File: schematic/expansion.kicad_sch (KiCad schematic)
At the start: 21 parts, among them J8 EXPANSION, U10 TPD4E05U06DQA, U11 TPD4E05U06DQA, U12 TPD4E05U06DQA, U13 TPD4E05U06DQA, U6 TPD4E05U06DQA, U7 TPD4E05U06DQA, U8 TPD4E05U06DQA, U9 TPD4E05U06DQA

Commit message: Rework for 8 nodes with MCP23017 relay drive
Target is now 8 motherboards per frame (was 14 in the schematic).

- relays_a/relays_b (14 channels, 28 photoMOS) replaced by one
  'Relay channels' sheet: 8 channels, 16 TLP176AM, J11-J18, same
  per-channel circuit and parts.
- U14 MCP23017 @0x20 drives the LEDs: GPA0-7 = PWR_DRV1-8,
  GPB0-7 = RST_DRV1-8. R32 pulls EXP_nRESET low so U14 stays in
  reset (all buttons released) unless the MCU drives it; R33 pulls
  up the shared open-drain EXP_INT.
- MCU: the two 14-bit drive buses are gone; PE2 = EXP_nRESET,
  PE3 = EXP_INT, the other 26 freed pins are no-connect.
- Expansion header J8 grows to 2x20 and carries I2C1, EXP_nRESET
  and EXP_INT (pins 5-8) for extra expander modules or a later
  power board, plus 3V3/5V on both ends.
- Net classes for the second relay bank removed; drive patterns
  point at the new sheet. Board regenerated (nothing placed).
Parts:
- removed J8: EXPANSION, Connector_PinHeader_2.54mm:PinHeader_2x18_P2.54mm_Vertical, symbol Connector_Generic:Conn_02x18_Odd_Even
- added J8: EXPANSION, Connector_PinHeader_2.54mm:PinHeader_2x20_P2.54mm_Vertical, symbol Connector_Generic:Conn_02x20_Odd_Even
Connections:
- net GND: now also J8.3 (Pin_3), J8.37 (Pin_37), J8.38 (Pin_38), J8.4 (Pin_4)
- net GPIO_PA0: now also RN2.8 (R1.2); no longer RN1.8 (R1.2)
- net GPIO_PA10: now also RN6.5 (R4.2); no longer RN6.7 (R2.2)
- net GPIO_PA15: now also RN5.5 (R4.2); no longer RN4.5 (R4.2)
- net GPIO_PA3: now also RN2.7 (R2.2); no longer RN1.7 (R2.2)
- net GPIO_PA4: now also RN2.6 (R3.2); no longer RN1.6 (R3.2)
- net GPIO_PA6: now also RN2.5 (R4.2); no longer RN1.5 (R4.2)
- net GPIO_PA8: now also RN6.6 (R3.2); no longer RN6.8 (R1.2)
- net GPIO_PB1: now also RN3.8 (R1.2); no longer RN2.8 (R1.2)
- net GPIO_PB10: now also RN7.6 (R3.2); no longer RN7.8 (R1.2)
- net GPIO_PB13: now also RN7.5 (R4.2); no longer RN7.7 (R2.2)
- net GPIO_PB14: now also RN8.8 (R1.2); no longer RN7.6 (R3.2)
- net GPIO_PB2: now also RN7.7 (R2.2); no longer RN6.5 (R4.2)
- net GPIO_PB4: now also RN7.8 (R1.2); no longer RN6.6 (R3.2)
- net GPIO_PB8: now also RN6.8 (R1.2); no longer RN5.6 (R3.2)
- net GPIO_PB9: now also RN6.7 (R2.2); no longer RN5.5 (R4.2)
- net GPIO_PC0: now also RN3.7 (R2.2); no longer RN2.7 (R2.2)
- net GPIO_PC10: now also RN5.8 (R1.2); no longer RN4.8 (R1.2)
- net GPIO_PC11: now also RN5.7 (R2.2); no longer RN4.7 (R2.2)
- net GPIO_PC12: now also RN5.6 (R3.2); no longer RN4.6 (R3.2)
- net GPIO_PC2: now also RN3.6 (R3.2); no longer RN2.6 (R3.2)
- net GPIO_PC3: now also RN3.5 (R4.2); no longer RN2.5 (R4.2)
- net GPIO_PC6: now also RN4.8 (R1.2); no longer RN3.8 (R1.2)
- net GPIO_PC7: now also RN4.7 (R2.2); no longer RN3.7 (R2.2)
- net GPIO_PC8: now also RN4.6 (R3.2); no longer RN3.6 (R3.2)
- net GPIO_PC9: now also RN4.5 (R4.2); no longer RN3.5 (R4.2)
- net GPIO_PD14: now also RN8.7 (R2.2); no longer RN7.5 (R4.2)
- net GPIO_PD15: now also RN8.6 (R3.2); no longer RN8.8 (R1.2)
- net GPIO_PE0: now also RN8.5 (R4.2); no longer RN8.7 (R2.2)
- net HDR_3V3: now also J8.1 (Pin_1), J8.39 (Pin_39)
- net HDR_5V: now also J8.2 (Pin_2), J8.40 (Pin_40)
- net HDR_PA0: now also RN2.1 (R1.1), U7.1 (D1+), J8.9 (Pin_9); no longer RN1.1 (R1.1), U6.1 (D1+)
- net HDR_PA10: now also RN6.4 (R4.1), U11.5 (D2-), J8.28 (Pin_28); no longer RN6.2 (R2.1), U11.2 (D1-)
- net HDR_PA15: now also RN5.4 (R4.1), U10.5 (D2-), J8.24 (Pin_24); no longer RN4.4 (R4.1), U9.5 (D2-)
- net HDR_PA3: now also RN2.2 (R2.1), U7.2 (D1-), J8.10 (Pin_10); no longer RN1.2 (R2.1), U6.2 (D1-)
- net HDR_PA4: now also RN2.3 (R3.1), U7.4 (D2+), J8.11 (Pin_11); no longer RN1.3 (R3.1), U6.4 (D2+)
- net HDR_PA6: now also RN2.4 (R4.1), U7.5 (D2-), J8.12 (Pin_12); no longer RN1.4 (R4.1), U6.5 (D2-)
- net HDR_PA8: now also RN6.3 (R3.1), U11.4 (D2+), J8.27 (Pin_27); no longer RN6.1 (R1.1), U11.1 (D1+)
- net HDR_PB1: now also RN3.1 (R1.1), U8.1 (D1+), J8.13 (Pin_13); no longer RN2.1 (R1.1), U7.1 (D1+)
- net HDR_PB10: now also RN7.3 (R3.1), U12.4 (D2+), J8.31 (Pin_31); no longer RN7.1 (R1.1), U12.1 (D1+)
- net HDR_PB13: now also RN7.4 (R4.1), U12.5 (D2-), J8.32 (Pin_32); no longer RN7.2 (R2.1), U12.2 (D1-)
- net HDR_PB14: now also RN8.1 (R1.1), U13.1 (D1+), J8.33 (Pin_33); no longer RN7.3 (R3.1), U12.4 (D2+)
- net HDR_PB2: now also RN7.2 (R2.1), U12.2 (D1-), J8.30 (Pin_30); no longer RN6.4 (R4.1), U11.5 (D2-)
- net HDR_PB4: now also RN7.1 (R1.1), U12.1 (D1+), J8.29 (Pin_29); no longer RN6.3 (R3.1), U11.4 (D2+)
- net HDR_PB8: now also RN6.1 (R1.1), U11.1 (D1+), J8.25 (Pin_25); no longer RN5.3 (R3.1), U10.4 (D2+)
- net HDR_PB9: now also RN6.2 (R2.1), U11.2 (D1-), J8.26 (Pin_26); no longer RN5.4 (R4.1), U10.5 (D2-)
- net HDR_PC0: now also RN3.2 (R2.1), U8.2 (D1-), J8.14 (Pin_14); no longer RN2.2 (R2.1), U7.2 (D1-)
- net HDR_PC10: now also RN5.1 (R1.1), U10.1 (D1+), J8.21 (Pin_21); no longer RN4.1 (R1.1), U9.1 (D1+)
- net HDR_PC11: now also RN5.2 (R2.1), U10.2 (D1-), J8.22 (Pin_22); no longer RN4.2 (R2.1), U9.2 (D1-)
- net HDR_PC12: now also RN5.3 (R3.1), U10.4 (D2+), J8.23 (Pin_23); no longer RN4.3 (R3.1), U9.4 (D2+)
- net HDR_PC2: now also RN3.3 (R3.1), U8.4 (D2+), J8.15 (Pin_15); no longer RN2.3 (R3.1), U7.4 (D2+)
- net HDR_PC3: now also RN3.4 (R4.1), U8.5 (D2-), J8.16 (Pin_16); no longer RN2.4 (R4.1), U7.5 (D2-)
- net HDR_PC6: now also RN4.1 (R1.1), U9.1 (D1+), J8.17 (Pin_17); no longer RN3.1 (R1.1), U8.1 (D1+)
- net HDR_PC7: now also RN4.2 (R2.1), U9.2 (D1-), J8.18 (Pin_18); no longer RN3.2 (R2.1), U8.2 (D1-)
- net HDR_PC8: now also RN4.3 (R3.1), U9.4 (D2+), J8.19 (Pin_19); no longer RN3.3 (R3.1), U8.4 (D2+)
- net HDR_PC9: now also RN4.4 (R4.1), U9.5 (D2-), J8.20 (Pin_20); no longer RN3.4 (R4.1), U8.5 (D2-)
- net HDR_PD14: now also RN8.2 (R2.1), U13.2 (D1-), J8.34 (Pin_34); no longer RN7.4 (R4.1), U12.5 (D2-)
- net HDR_PD15: now also RN8.3 (R3.1), U13.4 (D2+), J8.35 (Pin_35); no longer RN8.1 (R1.1), U13.1 (D1+)
- net HDR_PE0: now also RN8.4 (R4.1), U13.5 (D2-), J8.36 (Pin_36); no longer RN8.2 (R2.1), U13.2 (D1-)
- net HDR_SCL: now also RN1.1 (R1.1), U6.1 (D1+), J8.5 (Pin_5); no longer RN5.1 (R1.1), U10.1 (D1+)
- net HDR_SDA: now also RN1.2 (R2.1), U6.2 (D1-), J8.6 (Pin_6); no longer RN5.2 (R2.1), U10.2 (D1-)
- net I2C1_SCL: now also RN1.8 (R1.2); no longer RN5.8 (R1.2)
- net I2C1_SDA: now also RN1.7 (R2.2); no longer RN5.7 (R2.2)
- new net EXP_INT: RN1.5 (R4.2)
- new net EXP_nRESET: RN1.6 (R3.2)
- new net HDR_EXP_INT: J8.8 (Pin_8), RN1.4 (R4.1), U6.5 (D2-)
- new net HDR_EXP_nRESET: J8.7 (Pin_7), RN1.3 (R3.1), U6.4 (D2+)
- no-connect marks 38 -> 32
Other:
- note added: "Expansion header J8 (fit on demand). Every signal: 330R series (MCU side) + TPD4E05U06 ESD clamp at the pin. 330R limits a short to GND/3V3 or a 5V mis-wire to a few mA. Power pins: PTC fuse + TVS. Pins 5-8: I2C1 + EXP_nRESET + EXP_INT for extra MCP23017 modules (addr 0x21-0x27 by jumper) or a future power board. SPI3: PC10 SCK, PC11 MISO, PC12 MOSI, PA15 CS. USART6: PC6 TX, PC7 RX. FDCAN1: PB8 R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"
- note removed: "Expansion header J8 (fit on demand). Every signal: 330R series (MCU side) + TPD4E05U06 ESD clamp at the pin. 330R limits a short to GND/3V3 or a 5V mis-wire to a few mA. Power pins: PTC fuse + TVS. SPI3: PC10 SCK, PC11 MISO, PC12 MOSI, PA15 CS. USART6: PC6 TX, PC7 RX. FDCAN1: PB8 RX, PB9 TX. ADC: PA0 PA3 PA4 PA6 PB1 PC0 PC2 PC3. I2C1 (shared with U5 TMP1075). Verify AFs in CubeMX."

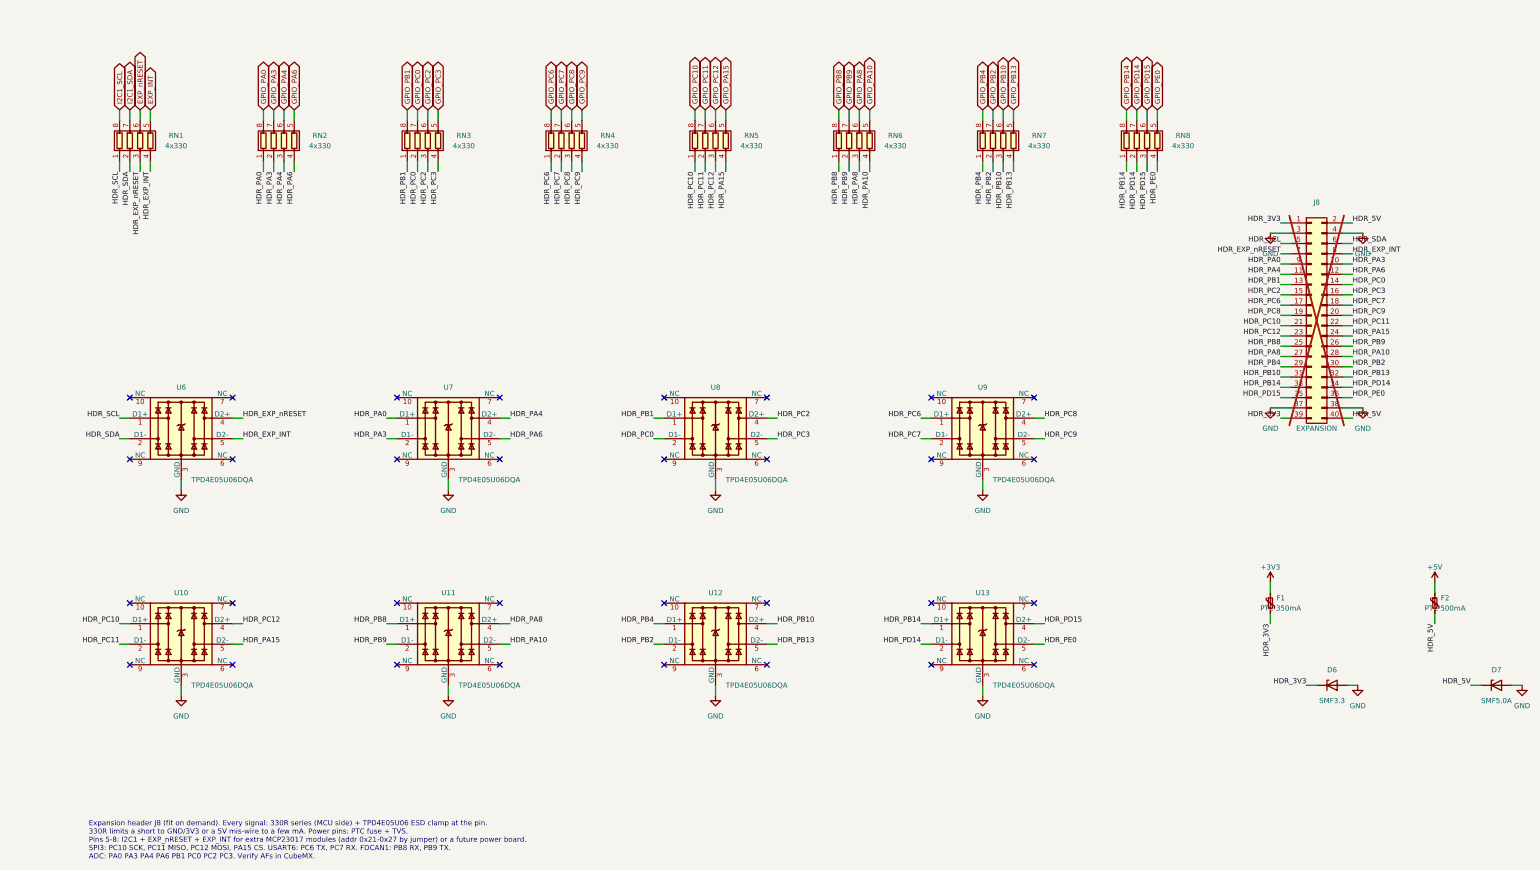
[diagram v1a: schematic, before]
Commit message: Rev C: ESP32-C6 + W5500 controller for immersion
Schematic rework per docs/controller.md.

- MCU: ESP32-C6-MINI-1-N4 replaces STM32H563VIT6 (KiCad-stock
  module). EN/BOOT test pads, USB-C via the C6 USB Serial/JTAG with
  22R series resistors behind the existing USBLC6.
- Ethernet: W5500 over SPI replaces LAN8742A/RMII. PHY network,
  center taps, AVDD ferrite and LED wiring per WIZnet's W5500
  Ethernet Shield reference; ARJP11A magjack and PoE path unchanged.
- I2C split: internal bus (relay MCP23017, TMP1075) on HP I2C with
  its own expander reset (EXP_nRESET_INT, GPIO14); external bus to
  the header (software I2C on GPIO6/7) with EXP_nRESET (GPIO4,
  pulled low) and the shared EXP_INT.
- Expansion header J8 now 2x6: external I2C, reset, interrupt,
  GPIO5/8/15, fused 3V3/5V, all protected as before.
- C1/C2: KEMET T520 molded tantalum-polymer instead of rubber-sealed
  aluminium-polymer cans (immersion).
- Sheets regenerated: Power, Ethernet, MCU replace power_eth and
  mcu_usb; root and project net classes updated (RMII/SWD/RST
  classes removed). Board regenerated, nothing placed yet.
- Spec updated to the captured design.
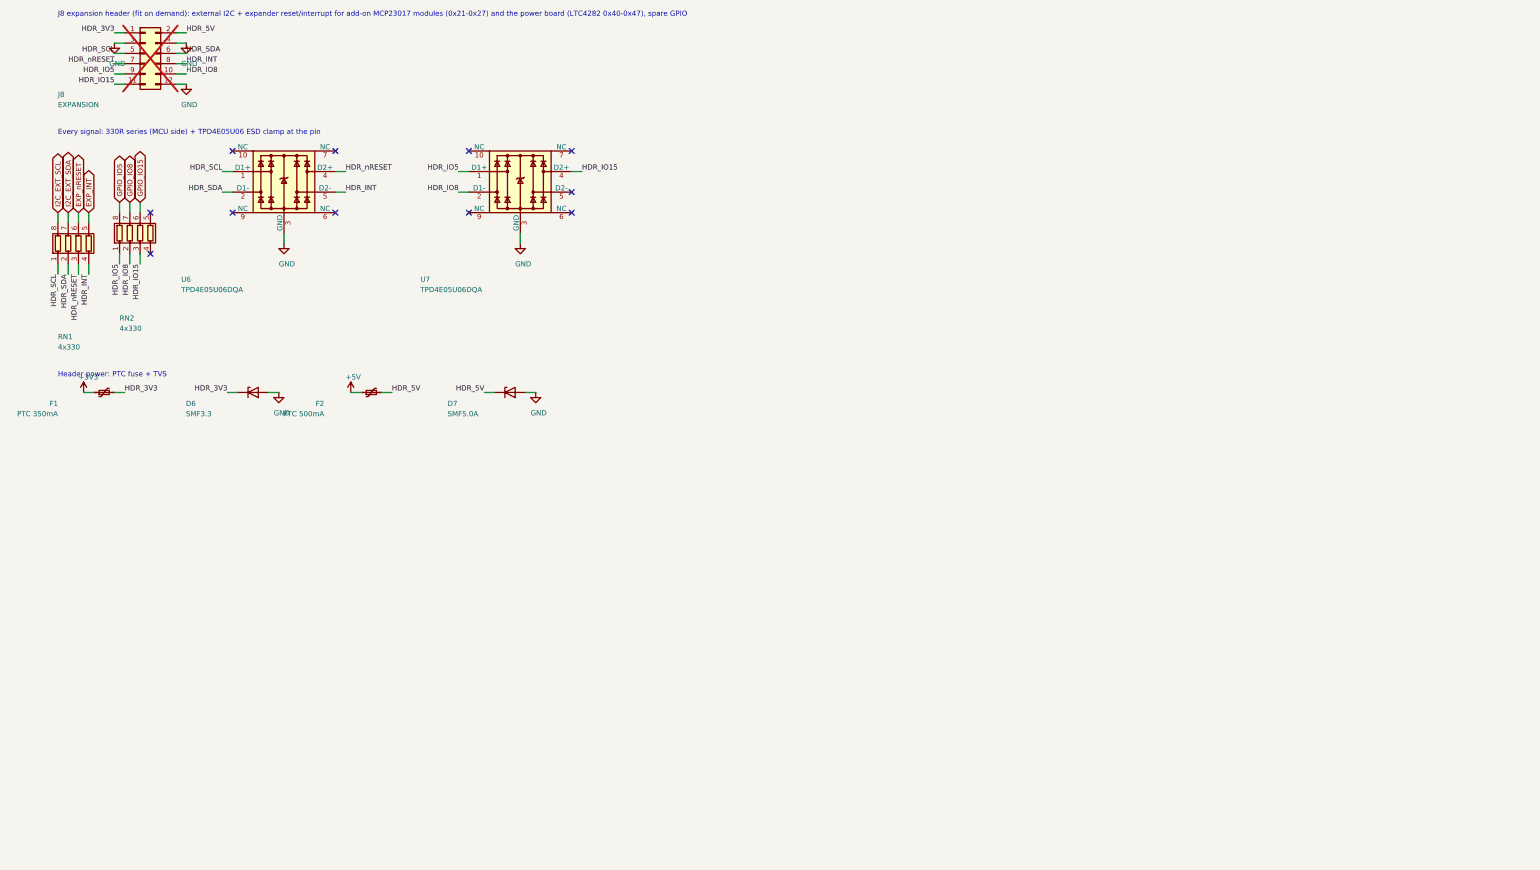
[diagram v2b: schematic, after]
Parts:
- removed J8: EXPANSION, Connector_PinHeader_2.54mm:PinHeader_2x20_P2.54mm_Vertical, symbol Connector_Generic:Conn_02x20_Odd_Even
- removed RN3, RN4, RN5, RN6, RN7, RN8: 4x330, Resistor_SMD:R_Array_Convex_4x0402, symbol Device:R_Pack04
- removed U10, U11, U12, U13, U8, U9: TPD4E05U06DQA, Package_SON:USON-10_2.5x1.0mm_P0.5mm, symbol Power_Protection:TPD4E05U06DQA
- added J8: EXPANSION, Connector_PinHeader_2.54mm:PinHeader_2x06_P2.54mm_Vertical, symbol Connector_Generic:Conn_02x06_Odd_Even
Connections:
- net GND: now also J8.12 (Pin_12), J8.3 (Pin_3), J8.4 (Pin_4)
- net HDR_3V3: now also J8.1 (Pin_1)
- net HDR_5V: now also J8.2 (Pin_2)
- net HDR_SCL: now also J8.5 (Pin_5)
- net HDR_SDA: now also J8.6 (Pin_6)
- net GPIO_PA0 renamed GPIO_IO5
- net GPIO_PA3 renamed GPIO_IO8
- net GPIO_PA4 renamed GPIO_IO15
- net GPIO_PA6: no longer names the net of RN2.5 (R4.2)
- net HDR_EXP_INT renamed HDR_INT
- net HDR_INT: now also J8.8 (Pin_8)
- net HDR_EXP_nRESET renamed HDR_nRESET
- net HDR_nRESET: now also J8.7 (Pin_7)
- net HDR_PA0 renamed HDR_IO5
- net HDR_IO5: now also J8.9 (Pin_9)
- net HDR_PA3 renamed HDR_IO8
- net HDR_IO8: now also J8.10 (Pin_10)
- net HDR_PA4 renamed HDR_IO15
- net HDR_IO15: now also J8.11 (Pin_11)
- net HDR_PA6: no longer names the net of RN2.4 (R4.1)
- net HDR_PA6: no longer U7.5 (D2-)
- net I2C1_SCL renamed I2C_EXT_SCL
- net I2C1_SDA renamed I2C_EXT_SDA
- no-connect marks 32 -> 11
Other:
- note added: "Every signal: 330R series (MCU side) + TPD4E05U06 ESD clamp at the pin"
- note added: "Header power: PTC fuse + TVS"
- note added: "J8 expansion header (fit on demand): external I2C + expander reset/interrupt for add-on MCP23017 modules (0x21-0x27) and the power board (LTC4282 0x40-0x47), spare GPIO"
- note removed: "Expansion header J8 (fit on demand). Every signal: 330R series (MCU side) + TPD4E05U06 ESD clamp at the pin. 330R limits a short to GND/3V3 or a 5V mis-wire to a few mA. Power pins: PTC fuse + TVS. Pins 5-8: I2C1 + EXP_nRESET + EXP_INT for extra MCP23017 modules (addr 0x21-0x27 by jumper) or a future power board. SPI3: PC10 SCK, PC11 MISO, PC12 MOSI, PA15 CS. USART6: PC6 TX, PC7 RX. FDCAN1: PB8 R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"
